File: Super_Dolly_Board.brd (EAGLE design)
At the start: 154.5 x 44.5 mm, 84 parts, among them J1 10118193-0001LF, J3 SJ1-2503A, J4 RJHS-538X, J5 SJ1-2503A, P1 TC33X-2, SW1 SKQUDBE010, U1 ATMEGA32U4-XUAU, U2 MMDT3904, U3 TB6559FG, U4 LM2937IMP-5.0/NOPB, U5 TB6559FG, U6 SN75176BDR, U7 TB6559FG, U8 TPD2E007DCK, U9 LM2937IMP-5.0/NOPB, X1 3.2X2.5MMCRYSTAL

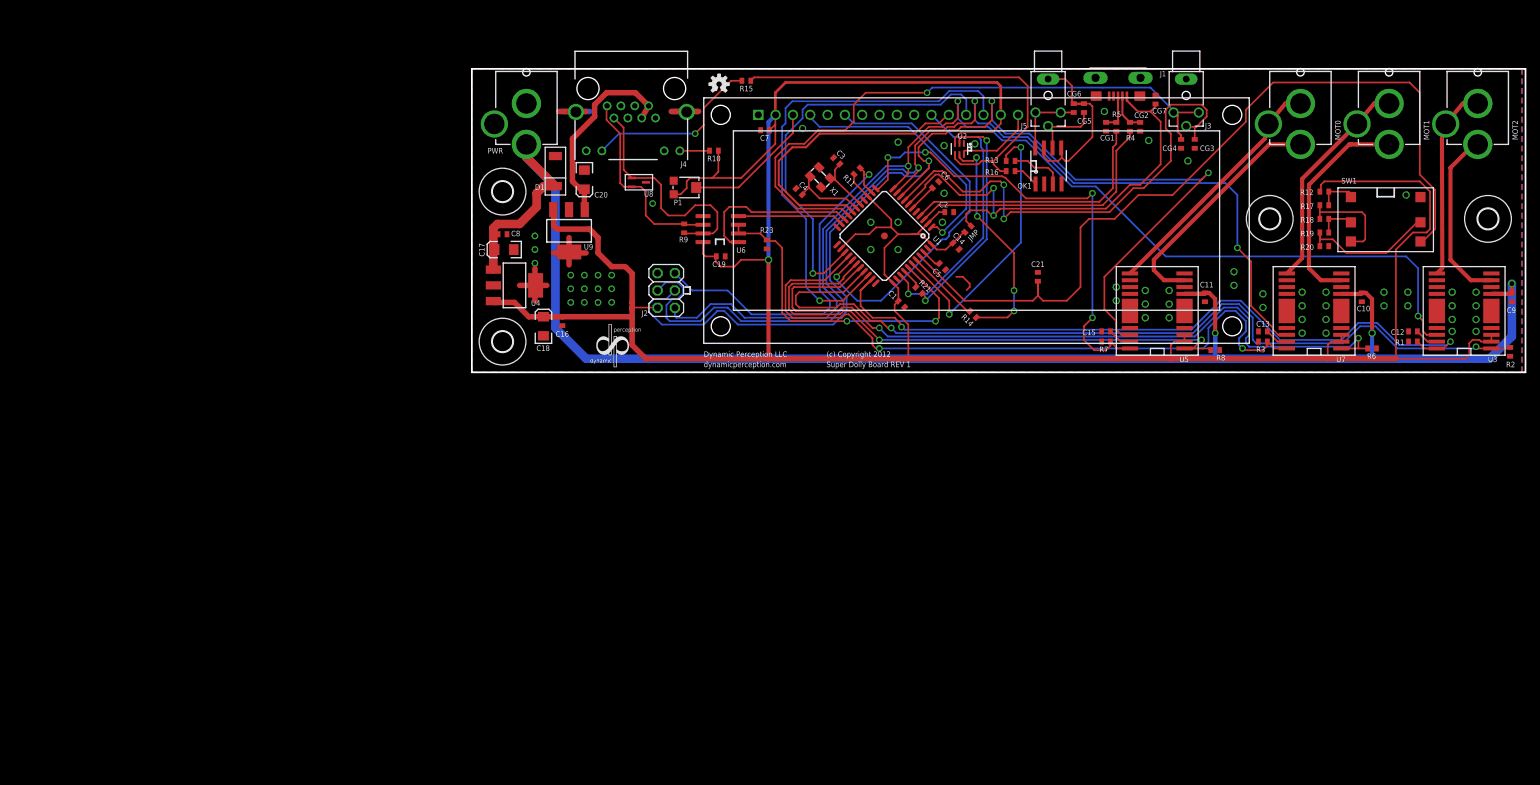
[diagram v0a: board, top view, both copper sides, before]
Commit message: checking in changed to the SDB and adding 2 libraries
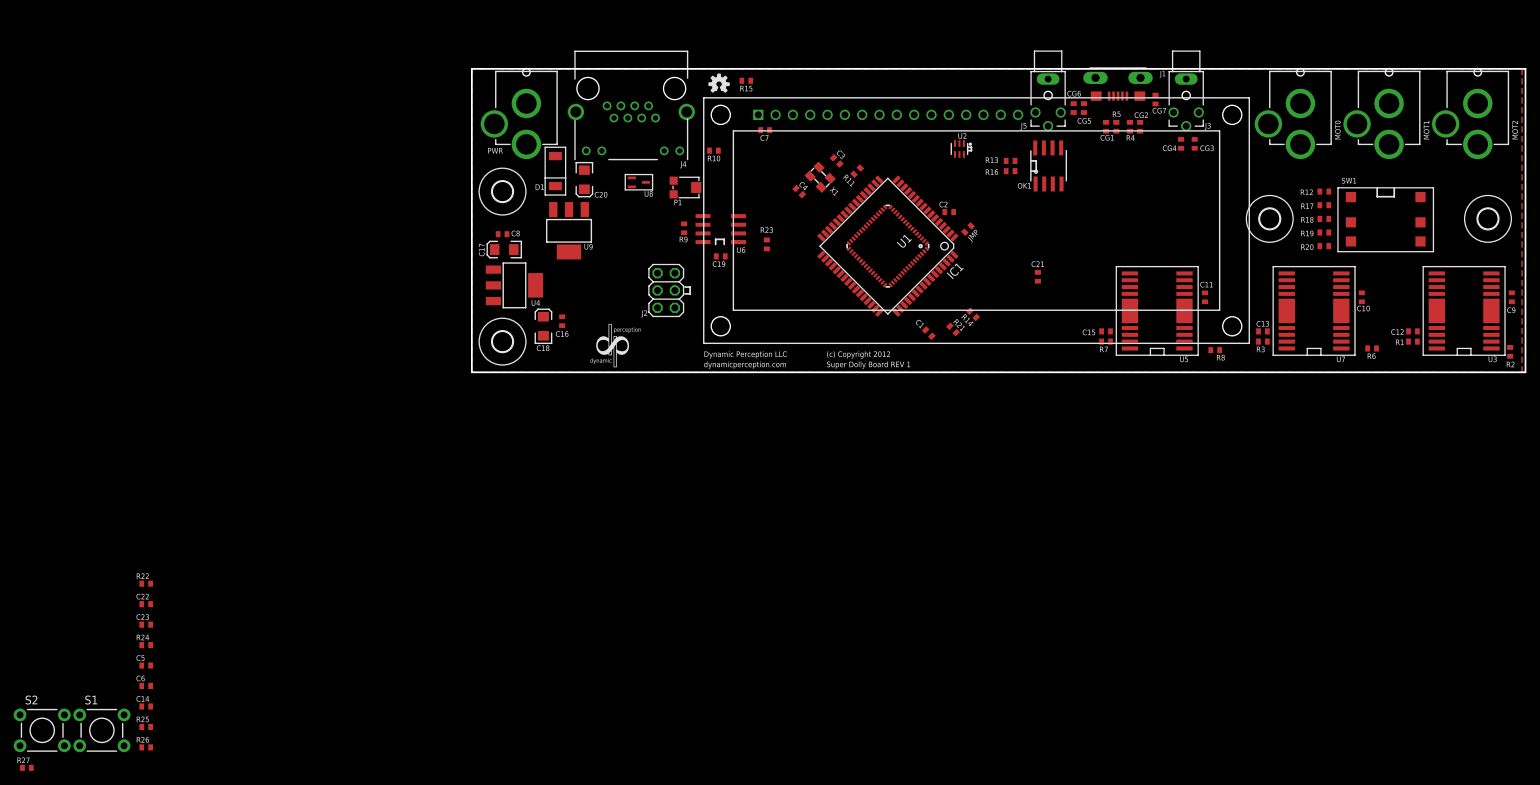
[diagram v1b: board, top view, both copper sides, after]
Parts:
- added C22: 1uF, parkers_parts:0402_CAP
- added C23: .1uF, parkers_parts:0402_CAP
- added IC1: AT90USB646-AU, at90usb:TQFP64
- added R22, R24: 0, parkers_parts:0402_RES
- added R25: 36K, parkers_parts:0402_RES
- added R26: 20K, parkers_parts:0402_RES
- added R27: 10K, parkers_parts:0402_RES
- added S1, S2: SKHHAJA010, SparkFun-Electromechanical:TACTILE-PTH
- C14, C6: value 1uF -> .1uF
- U1: value ATMEGA32U4-XUAU -> AT90USB646-MU; device SmartPrj:TQFP44-PAD -> at90usb:MLF64
- U4, U9: value LM2937IMP-5.0/NOPB -> TS2937CW50
- moved C6 137.1 mm to (-121.8, -71.5), turned to 0 degrees
- moved C14 136.6 mm to (-121.8, -74.5), turned to 0 degrees
- moved C5 130.6 mm to (-121.8, -68.5), turned to 0 degrees
- moved R21 7.62 mm to (-3.44, -19.2)
- moved C1 5.84 mm to (-7.00, -19.8)
- moved U1 1.58 mm to (-13.0, -7.00)
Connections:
- removed net D0/RX: U1.20, U6.1
- removed net D1/TX: U1.21, U6.4
- removed net HWB: U1.33
- removed net MISO/M2_P: J2.1, U1.11, U3.14
- removed net MOSI/M1_P: J2.4, U1.10, U7.14
- removed net RESET: J2.5, R11.2, U1.13
- removed net RXLED/IO_2: CG3.2, J3.4, U1.8
- removed net SCK/M0_P: J2.3, U1.9, U5.14
- removed net TXLED: U1.22
- removed net XTAL1: C4.2, U1.17, X1.3
- removed net XTAL2: C3.2, U1.16, X1.1
- new net AGND: C23.2, IC1.63, R24.2, U1.63
- new net BATT_V: IC1.60, R25.1, R26.2, U1.60
- new net IO_0: IC1.14, U1.14
- new net IO_1: IC1.15, U1.15
- new net IO_2: CG3.2, IC1.16, J3.4, U1.16
- new net M0_P: IC1.51, U1.51, U5.14
- new net M1_P: IC1.50, U1.50, U7.14
- new net M2_P: IC1.49, U1.49, U3.14
- new net MISO: IC1.13, J2.1, U1.13
- new net MOSI: IC1.12, J2.4, U1.12
- new net PC7: IC1.42, U1.42
- new net PE0: IC1.33, U1.33
- new net PE1: IC1.34, U1.34
- new net PE2: IC1.43, R27.2, S2.1, U1.43
- new net PE3: IC1.9, U1.9
- new net PE4: IC1.18, U1.18
- new net PE5: IC1.19, U1.19
- new net PE6: IC1.1, U1.1
- new net PE7: IC1.2, U1.2
- new net PF2: IC1.59, U1.59
- new net PF3: IC1.58, U1.58
- new net PF4: IC1.57, U1.57
- new net PF5: IC1.56, U1.56
- new net PF6: IC1.55, U1.55
- new net PF7: IC1.54, U1.54
- new net RST: IC1.20, J2.5, R11.2, S1.1, U1.20
- new net RX: IC1.27, U1.27, U6.1
- new net SCK: IC1.11, J2.3, U1.11
- new net TX: IC1.28, U1.28, U6.4
- new net UGND: C22.1, CG1.1, CG2.1, CG7.1, IC1.6, J1.5, J1.S1, J1.S2, J1.S3, J1.S4, R22.1, U1.6
- new net X1: C4.2, IC1.24, U1.24, X1.3
- new net X2: C3.2, IC1.23, U1.23, X1.1
- net +5V: now also C5.1, C6.1, IC1.21, IC1.3, IC1.52, IC1.64, R27.1, U1.21, U1.3, U1.52, U1.64; no longer U1.14, U1.2, U1.24, U1.34, U1.44
- net AREF: now also C23.1, IC1.62, U1.62; no longer C5.1, U1.42
- net BTNS: now also IC1.61, U1.61; no longer U1.41
- net COM1: now also IC1.25, U1.25
- net COM2: now also IC1.26, U1.26
- net COM3: now also IC1.32, U1.32
- net DE: now also IC1.29, U1.29; no longer U1.38
- net FOC: now also IC1.31, U1.31; no longer U1.39
- net GND: now also IC1.22, IC1.53, R22.2, R24.1, R26.1, S1.3, S2.3, U1.22, U1.53; no longer CG1.1, CG2.1, CG7.1, J1.5, J1.S1, J1.S2, J1.S3, J1.S4, U1.15, U1.23, U1.35, U1.43, U1.5, U1.P$1
- net IO_3: now also IC1.17, U1.17; no longer U1.19
- net LCD_BK: now also IC1.41, U1.41; no longer U1.37
- net LCD_D4: now also IC1.35, U1.35; no longer U1.36
- net LCD_D5: now also IC1.36, U1.36; no longer U1.18
- net LCD_D6: now also IC1.37, U1.37; no longer U1.25
- net LCD_D7: now also IC1.38, U1.38; no longer U1.31
- net LCD_E: now also IC1.39, U1.39; no longer U1.27
- net LCD_RS: now also IC1.40, U1.40; no longer U1.1
- net M0_A: now also IC1.48, U1.48; no longer U1.28
- net M0_B: now also IC1.45, U1.45; no longer U1.12
- net M1_A: now also IC1.47, U1.47; no longer U1.29
- net M1_B: now also IC1.44, U1.44; no longer U1.26
- net M2_A: now also IC1.46, U1.46; no longer U1.30
- net M2_B: now also IC1.10, U1.10; no longer U1.32
- net RD+: now also IC1.5, U1.5; no longer U1.4
- net RD-: now also IC1.4, U1.4; no longer U1.3
- net SHT: now also IC1.30, U1.30; no longer U1.40
- net UCAP: now also C22.2, IC1.7, U1.7; no longer C6.1, U1.6
- net VIN: now also R25.2
- net VUSB: now also IC1.8, U1.8; no longer U1.7
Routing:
- net +5V: track 429.1 -> 0.00 mm, vias 1 -> 0
- net VIN: track 249.5 -> 0.00 mm, vias 3 -> 0
- net SCK/M0_P: track 166.3 -> 0.00 mm, vias 3 -> 0
- net MISO/M2_P: track 165.4 -> 0.00 mm, vias 3 -> 0
- net MOSI/M1_P: track 160.6 -> 0.00 mm, vias 3 -> 0
- net M2_A: track 128.6 -> 0.00 mm, vias 2 -> 0
- net BTNS: track 124.8 -> 0.00 mm
- net M1_A: track 111.9 -> 0.00 mm, vias 2 -> 0
- net M2_B: track 107.5 -> 0.00 mm, vias 2 -> 0
- net M1_B: track 102.3 -> 0.00 mm, vias 2 -> 0
- net IO_3: track 90.8 -> 0.00 mm, vias 1 -> 0
- net M0_A: track 84.5 -> 0.00 mm, vias 2 -> 0
- net LCD_D7: track 72.5 -> 0.00 mm, vias 1 -> 0
- net RXLED/IO_2: track 72.3 -> 0.00 mm, vias 2 -> 0
- net M0_B: track 69.6 -> 0.00 mm, vias 4 -> 0
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
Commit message: finished routing. needs optimizing for SDB
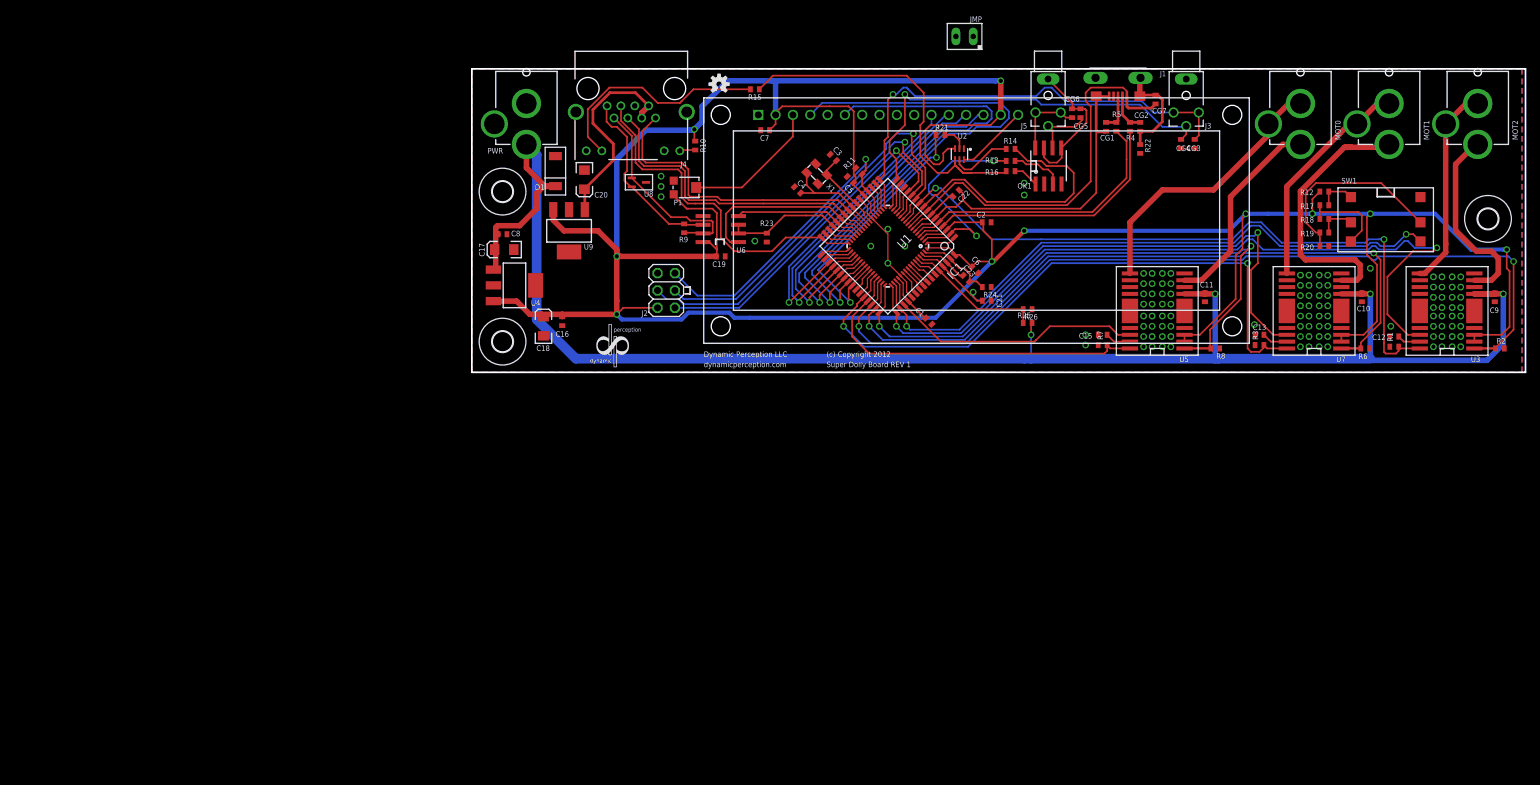
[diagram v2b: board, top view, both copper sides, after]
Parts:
- removed C14: .1uF, parkers_parts:0402_CAP
- removed H3: MOUNT-HOLE3.0, holes:3,0
- removed R27: 10K, parkers_parts:0402_RES
- removed S1, S2: SKHHAJA010, SparkFun-Electromechanical:TACTILE-PTH
- JMP: value (none) -> P1X02PH; device parkers_parts:0402_RES -> parkers_parts:P1X02
- moved R22 159.1 mm to (24.0, 7.25), turned to 270 degrees
- moved R26 144.3 mm to (7.50, -16.2), turned to 180 degrees
- moved R25 142.2 mm to (7.50, -18.2)
- moved C6 136.0 mm to (-0.25, -10.5), turned to 315 degrees
- moved R24 134.0 mm to (1.50, -13.0), turned to 180 degrees
- moved C22 133.2 mm to (-3.00, 0.75), turned to 225 degrees
- moved C23 130.5 mm to (-1.50, -11.8), turned to 315 degrees
- moved C5 125.4 mm to (-18.5, 2.75), turned to 135 degrees
- moved R21 28.6 mm to (-5.29, 9.31), turned to 0 degrees
- moved JMP 28.3 mm to (-1.75, 23.8), turned to 180 degrees
- moved R14 24.9 mm to (5.00, 7.25), turned to 180 degrees
- moved C21 8.28 mm to (1.50, -15.0), turned to 180 degrees
- moved C2 5.69 mm to (1.49, -3.50)
- moved C12 2.85 mm to (61.2, -20.2)
- moved R1 2.85 mm to (61.2, -21.8)
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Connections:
- removed net PE3: IC1.9, U1.9
- removed net PE7: IC1.2, U1.2
- new net PD5: IC1.30, U1.30
- new net PD6: IC1.31, U1.31
- net +5V: now also JMP.2; no longer C14.1, JMP.1, R27.1
- net COM1: now also IC1.32, U1.32; no longer IC1.25, U1.25
- net COM3: now also IC1.25, U1.25; no longer IC1.32, U1.32
- net FOC: now also IC1.2, U1.2; no longer IC1.31, U1.31
- net GND: no longer C14.2, S1.3, S2.3
- net PE2: no longer R27.2, S2.1
- net RST: no longer S1.1
- net SHT: now also IC1.9, U1.9; no longer IC1.30, U1.30
- net VUSB: now also JMP.1; no longer JMP.2
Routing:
- net +5V: track 0.00 -> 473.1 mm, vias 0 -> 10
- net VIN: track 0.00 -> 249.0 mm, vias 0 -> 4
- net M2_A: track 0.00 -> 131.5 mm, vias 0 -> 2
- net M2_P: track 0.00 -> 114.2 mm, vias 0 -> 2
- net M1_A: track 0.00 -> 110.3 mm, vias 0 -> 2
- net M2_B: track 0.00 -> 101.2 mm, vias 0 -> 2
- net M1_B: track 0.00 -> 94.3 mm, vias 0 -> 2
- net M0_A: track 0.00 -> 92.1 mm, vias 0 -> 2
- net BTNS: track 0.00 -> 86.3 mm, vias 0 -> 2
- net M1_P: track 0.00 -> 83.6 mm, vias 0 -> 2
- net LCD_RS: track 0.00 -> 82.9 mm, vias 0 -> 1
- net LCD_E: track 0.00 -> 74.1 mm, vias 0 -> 1
- net IO_3: track 0.00 -> 69.8 mm, vias 0 -> 1
- net UGND: track 0.00 -> 67.8 mm
- net IO_2: track 0.00 -> 63.8 mm, vias 0 -> 1
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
